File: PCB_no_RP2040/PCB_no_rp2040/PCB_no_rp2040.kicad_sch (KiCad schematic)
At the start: 46 parts, among them J1 02x30_Shift_Register_Connector, J2 02x30_Shift_Register_Connector, U1 74HC595, U2 74HC595, U3 74HC595, U4 74HC595, U5 74HC595, U6 74HC595, U7 74HC595, U8 MAX11643EEG, U9 MAX11643EEG

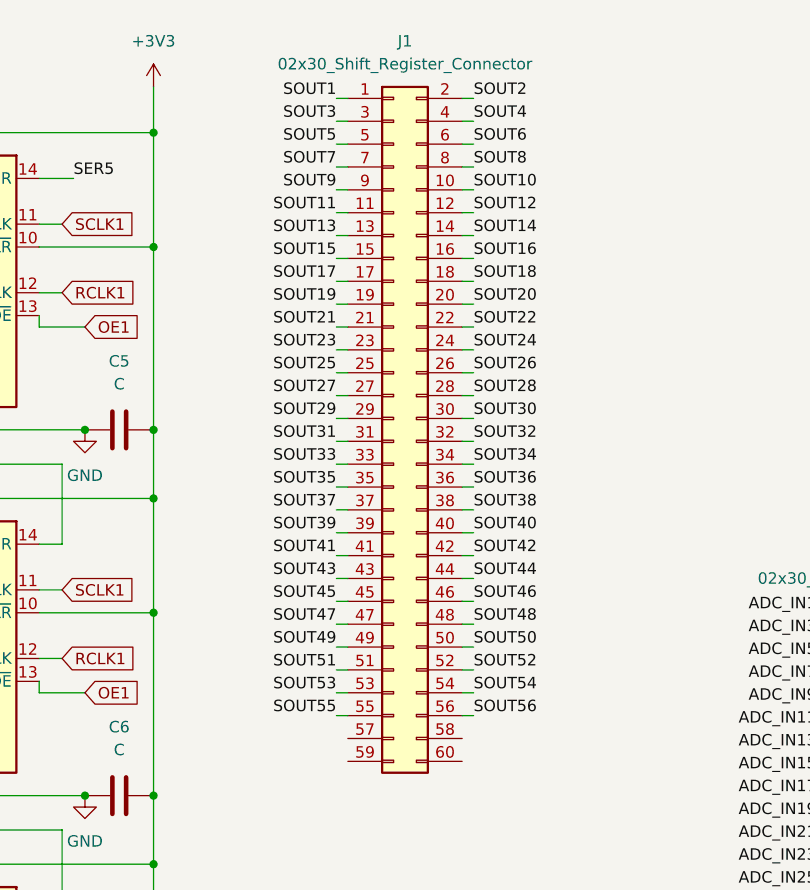
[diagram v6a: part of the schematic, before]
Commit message: added diodes to between all shift register outputs and the connector
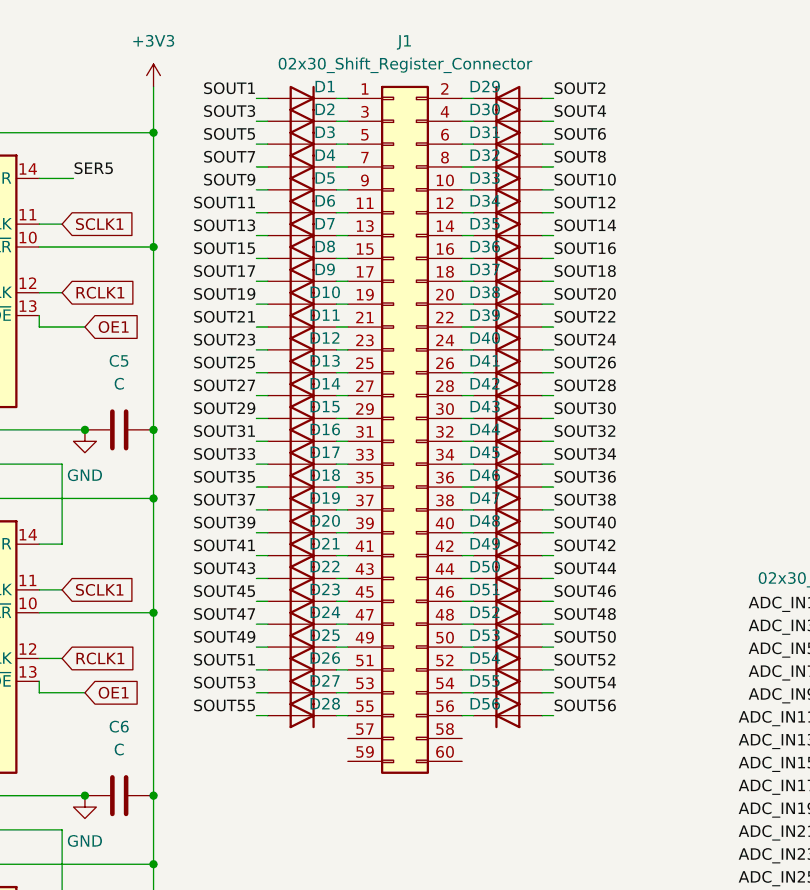
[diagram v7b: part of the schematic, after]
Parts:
- added D1, D10, D11, D12, D13, D14, D15, D16, D17, D18, D19, D2, D20, D21, D22, D23, D24, D25, D26, D27, D28, D29, D3, D30, D31, D32, D33, D34, D35, D36, D37, D38, D39, D4, D40, D41, D42, D43, D44, D45, D46, D47, D48, D49, D5, D50, D51, D52, D53, D54, D55, D56, D6, D7, D8, D9: D, symbol Device:D
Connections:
- net SOUT1: now also D1.2 (A); no longer J1.1 (Pin_1)
- net SOUT10: now also D33.2 (A); no longer J1.10 (Pin_10)
- net SOUT11: now also D6.2 (A); no longer J1.11 (Pin_11)
- net SOUT12: now also D34.2 (A); no longer J1.12 (Pin_12)
- net SOUT13: now also D7.2 (A); no longer J1.13 (Pin_13)
- net SOUT14: now also D35.2 (A); no longer J1.14 (Pin_14)
- net SOUT15: now also D8.2 (A); no longer J1.15 (Pin_15)
- net SOUT16: now also D36.2 (A); no longer J1.16 (Pin_16)
- net SOUT17: now also D9.2 (A); no longer J1.17 (Pin_17)
- net SOUT18: now also D37.2 (A); no longer J1.18 (Pin_18)
- net SOUT19: now also D10.2 (A); no longer J1.19 (Pin_19)
- net SOUT2: now also D29.2 (A); no longer J1.2 (Pin_2)
- net SOUT20: now also D38.2 (A); no longer J1.20 (Pin_20)
- net SOUT21: now also D11.2 (A); no longer J1.21 (Pin_21)
- net SOUT22: now also D39.2 (A); no longer J1.22 (Pin_22)
- net SOUT23: now also D12.2 (A); no longer J1.23 (Pin_23)
- net SOUT24: now also D40.2 (A); no longer J1.24 (Pin_24)
- net SOUT25: now also D13.2 (A); no longer J1.25 (Pin_25)
- net SOUT26: now also D41.2 (A); no longer J1.26 (Pin_26)
- net SOUT27: now also D14.2 (A); no longer J1.27 (Pin_27)
- net SOUT28: now also D42.2 (A); no longer J1.28 (Pin_28)
- net SOUT29: now also D15.2 (A); no longer J1.29 (Pin_29)
- net SOUT3: now also D2.2 (A); no longer J1.3 (Pin_3)
- net SOUT30: now also D43.2 (A); no longer J1.30 (Pin_30)
- net SOUT31: now also D16.2 (A); no longer J1.31 (Pin_31)
- net SOUT32: now also D44.2 (A); no longer J1.32 (Pin_32)
- net SOUT33: now also D17.2 (A); no longer J1.33 (Pin_33)
- net SOUT34: now also D45.2 (A); no longer J1.34 (Pin_34)
- net SOUT35: now also D18.2 (A); no longer J1.35 (Pin_35)
- net SOUT36: now also D46.2 (A); no longer J1.36 (Pin_36)
- net SOUT37: now also D19.2 (A); no longer J1.37 (Pin_37)
- net SOUT38: now also D47.2 (A); no longer J1.38 (Pin_38)
- net SOUT39: now also D20.2 (A); no longer J1.39 (Pin_39)
- net SOUT4: now also D30.2 (A); no longer J1.4 (Pin_4)
- net SOUT40: now also D48.2 (A); no longer J1.40 (Pin_40)
- net SOUT41: now also D21.2 (A); no longer J1.41 (Pin_41)
- net SOUT42: now also D49.2 (A); no longer J1.42 (Pin_42)
- net SOUT43: now also D22.2 (A); no longer J1.43 (Pin_43)
- net SOUT44: now also D50.2 (A); no longer J1.44 (Pin_44)
- net SOUT45: now also D23.2 (A); no longer J1.45 (Pin_45)
- net SOUT46: now also D51.2 (A); no longer J1.46 (Pin_46)
- net SOUT47: now also D24.2 (A); no longer J1.47 (Pin_47)
- net SOUT48: now also D52.2 (A); no longer J1.48 (Pin_48)
- net SOUT49: now also D25.2 (A); no longer J1.49 (Pin_49)
- net SOUT5: now also D3.2 (A); no longer J1.5 (Pin_5)
- net SOUT50: now also D53.2 (A); no longer J1.50 (Pin_50)
- net SOUT51: now also D26.2 (A); no longer J1.51 (Pin_51)
- net SOUT52: now also D54.2 (A); no longer J1.52 (Pin_52)
- net SOUT53: now also D27.2 (A); no longer J1.53 (Pin_53)
- net SOUT54: now also D55.2 (A); no longer J1.54 (Pin_54)
- net SOUT55: now also D28.2 (A); no longer J1.55 (Pin_55)
- net SOUT56: now also D56.2 (A); no longer J1.56 (Pin_56)
- net SOUT6: now also D31.2 (A); no longer J1.6 (Pin_6)
- net SOUT7: now also D4.2 (A); no longer J1.7 (Pin_7)
- net SOUT8: now also D32.2 (A); no longer J1.8 (Pin_8)
- net SOUT9: now also D5.2 (A); no longer J1.9 (Pin_9)
- new net: D54.1 (K), J1.52 (Pin_52)
- new net: D47.1 (K), J1.38 (Pin_38)
- new net: D17.1 (K), J1.33 (Pin_33)
- new net: D9.1 (K), J1.17 (Pin_17)
- new net: D20.1 (K), J1.39 (Pin_39)
- new net: D53.1 (K), J1.50 (Pin_50)
- new net: D19.1 (K), J1.37 (Pin_37)
- new net: D29.1 (K), J1.2 (Pin_2)
- new net: D51.1 (K), J1.46 (Pin_46)
- new net: D2.1 (K), J1.3 (Pin_3)
- new net: D41.1 (K), J1.26 (Pin_26)
- new net: D1.1 (K), J1.1 (Pin_1)
- new net: D55.1 (K), J1.54 (Pin_54)
- new net: D16.1 (K), J1.31 (Pin_31)
- new net: D33.1 (K), J1.10 (Pin_10)
- new net: D6.1 (K), J1.11 (Pin_11)
- new net: D34.1 (K), J1.12 (Pin_12)
- new net: D7.1 (K), J1.13 (Pin_13)
- new net: D35.1 (K), J1.14 (Pin_14)
- new net: D8.1 (K), J1.15 (Pin_15)
- new net: D36.1 (K), J1.16 (Pin_16)
- new net: D37.1 (K), J1.18 (Pin_18)
- new net: D10.1 (K), J1.19 (Pin_19)
- new net: D38.1 (K), J1.20 (Pin_20)
- new net: D11.1 (K), J1.21 (Pin_21)
- new net: D39.1 (K), J1.22 (Pin_22)
- new net: D12.1 (K), J1.23 (Pin_23)
- new net: D40.1 (K), J1.24 (Pin_24)
- new net: D13.1 (K), J1.25 (Pin_25)
- new net: D14.1 (K), J1.27 (Pin_27)
- new net: D42.1 (K), J1.28 (Pin_28)
- new net: D15.1 (K), J1.29 (Pin_29)
- new net: D43.1 (K), J1.30 (Pin_30)
- new net: D44.1 (K), J1.32 (Pin_32)
- new net: D45.1 (K), J1.34 (Pin_34)
- new net: D18.1 (K), J1.35 (Pin_35)
- new net: D46.1 (K), J1.36 (Pin_36)
- new net: D30.1 (K), J1.4 (Pin_4)
- new net: D48.1 (K), J1.40 (Pin_40)
- new net: D21.1 (K), J1.41 (Pin_41)
- new net: D49.1 (K), J1.42 (Pin_42)
- new net: D22.1 (K), J1.43 (Pin_43)
- new net: D50.1 (K), J1.44 (Pin_44)
- new net: D23.1 (K), J1.45 (Pin_45)
- new net: D24.1 (K), J1.47 (Pin_47)
- new net: D52.1 (K), J1.48 (Pin_48)
- new net: D25.1 (K), J1.49 (Pin_49)
- new net: D3.1 (K), J1.5 (Pin_5)
- new net: D26.1 (K), J1.51 (Pin_51)
- new net: D27.1 (K), J1.53 (Pin_53)
- new net: D28.1 (K), J1.55 (Pin_55)
- new net: D56.1 (K), J1.56 (Pin_56)
- new net: D31.1 (K), J1.6 (Pin_6)
- new net: D4.1 (K), J1.7 (Pin_7)
- new net: D32.1 (K), J1.8 (Pin_8)
- new net: D5.1 (K), J1.9 (Pin_9)

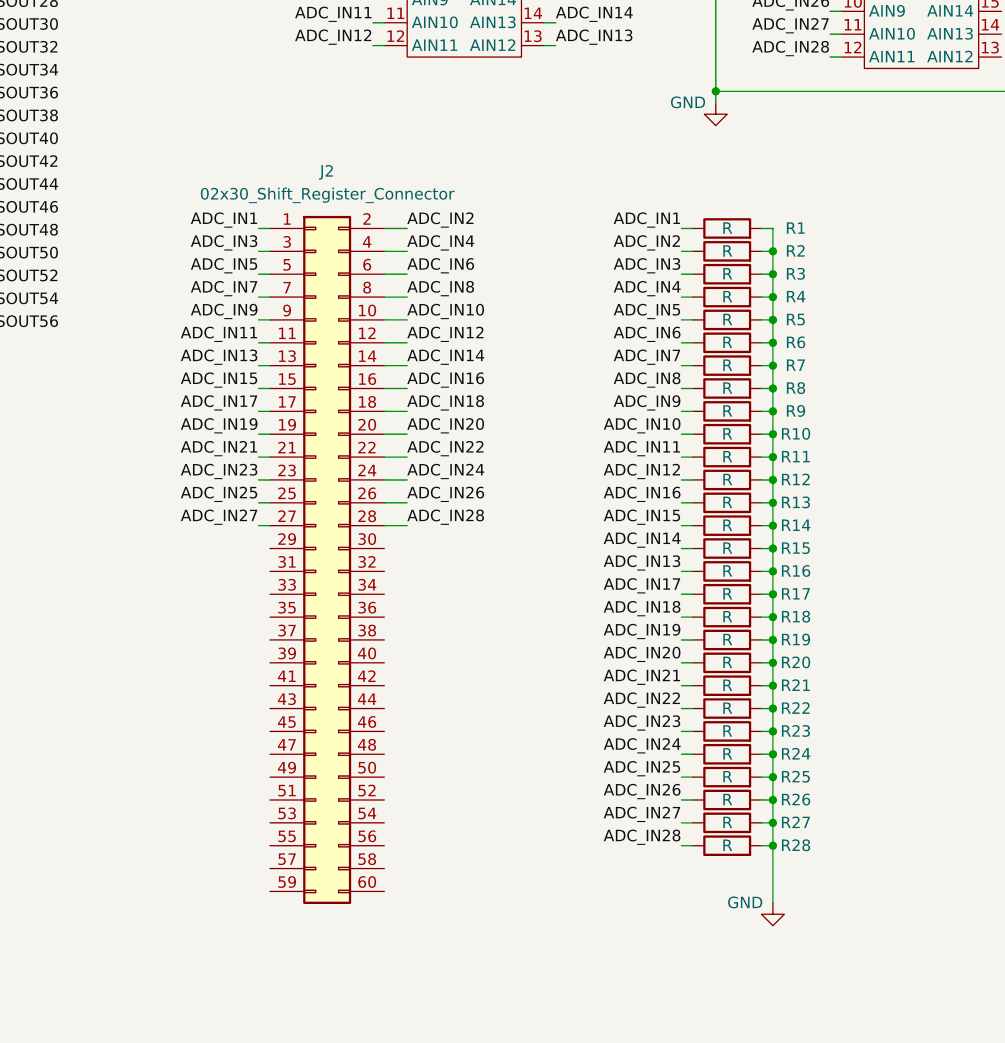
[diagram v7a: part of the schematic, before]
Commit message: changed name of ADC connector, added box w text to voltage divider as visual aid
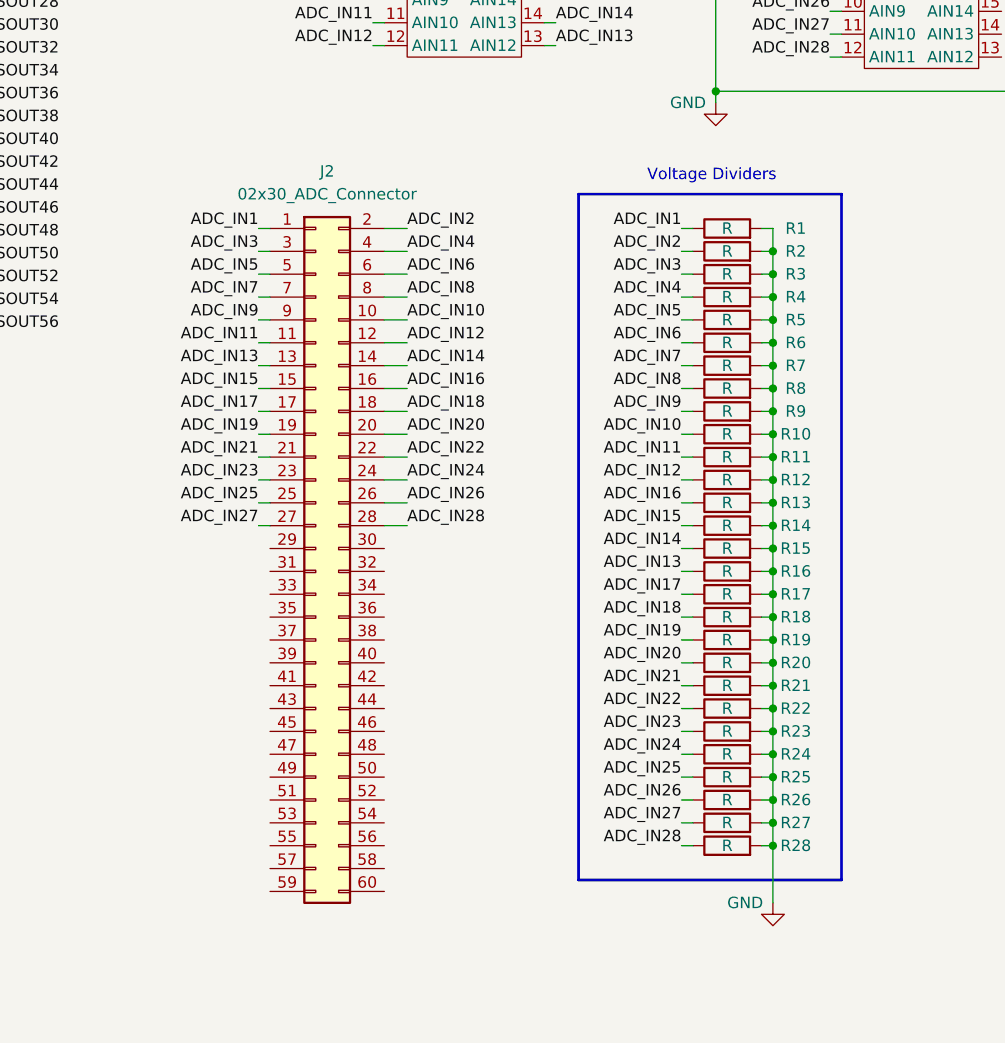
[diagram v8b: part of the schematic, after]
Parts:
- J2: value 02x30_Shift_Register_Connector -> 02x30_ADC_Connector
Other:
- note added: "Voltage Dividers"
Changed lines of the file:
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@@
     (stroke (width 0) (type default))
   )
+  (rectangle (start 214.63 74.93) (end 243.84 151.13)
+    (stroke (width 0.3) (type default) (color 0 0 0 1))
+    (fill (type none))
+  )
+  (text "Voltage Dividers" (at 222.25 73.66 0)
+    (effects (font (size 1.27 1.27)) (justify left bottom))
+  )
   (label "ADC_IN14" (at 212.09 55.88 0) (fields_autoplaced)
     (effects (font (size 1.27 1.27)) (justify left bottom))
@@
       (effects (font (size 1.27 1.27)))
     )
-    (property "Value" "02x30_Shift_Register_Connector" (at 186.69 74.93 0)
+    (property "Value" "02x30_ADC_Connector" (at 186.69 74.93 0)
       (effects (font (size 1.27 1.27)))
     )
